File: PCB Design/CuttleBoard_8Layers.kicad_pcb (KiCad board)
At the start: 8 copper layers, 50 x 50 mm, 178 parts, among them IC1 W25Q256JVEIQ TR, J1 DX07WH24JA3R1200, SW1 SW_Push, SW2 SW_Push, U1 LMR33630CQRNX, U14 STM32H743VIHx, U15 TPS62824ADMQ, U16 ICM-20602, U19 USBLC6-2P6, U20 ACS722xLCTR-10AB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

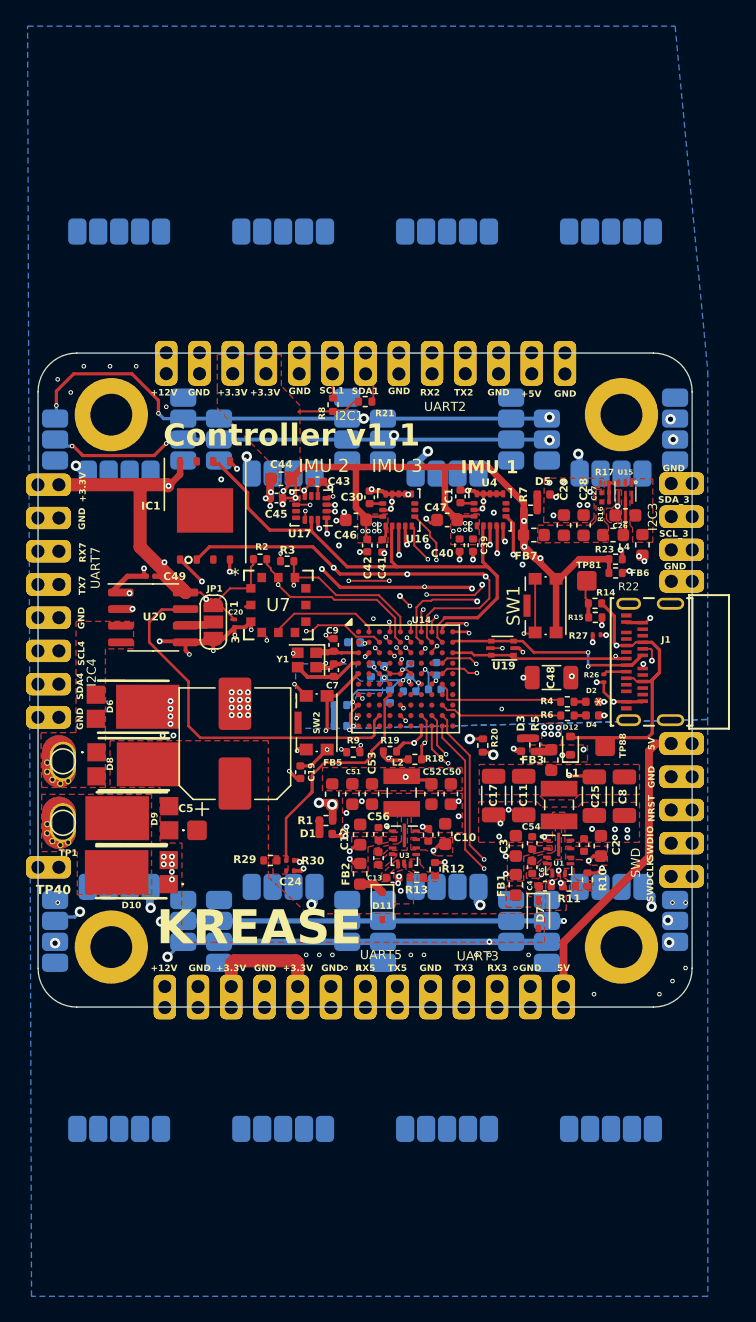
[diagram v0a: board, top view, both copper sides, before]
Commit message: via size 0.35mm to 0.45mm
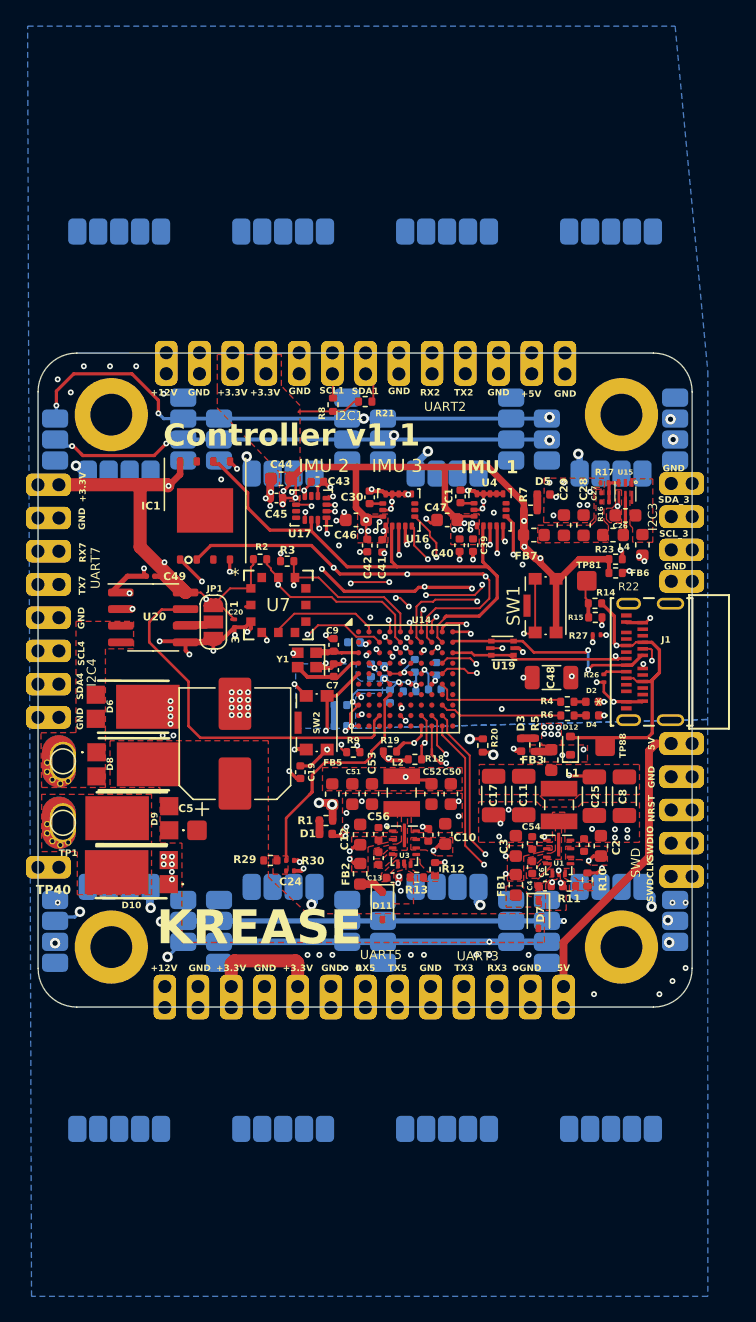
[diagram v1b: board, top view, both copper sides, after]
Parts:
- moved C32 0.47 mm to (126.3, 97.9)
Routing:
- net SPI3_MOSI: track 44.6 -> 45.6 mm
- net +3.3V: track 164.3 -> 165.1 mm, vias 35 -> 34
- net UART2_TX: track 26.4 -> 27.0 mm
- net USB_D+: track 16.3 -> 16.9 mm
- net INT1_IMU3: track 17.3 -> 17.8 mm
